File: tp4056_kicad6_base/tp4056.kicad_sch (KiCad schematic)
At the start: 33 parts, among them J1 Conn_01x01_Female, J2 Conn_01x01_Female, J3 USB_B_Micro, J4 Conn_01x02_Male, J6 Conn_01x05_Male, Q1 AO3401A, Q2 FS8205A, Q3 AO3401A, U1 TP4056, U2 DW01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

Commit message: SCH. Add USB and Wall Power Adaptor
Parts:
- added D4: MBR1020VL, Diode_SMD_AKL:D_SOD-123F, symbol Diode:MBR1020VL
- added Q4: AO3401A, Package_TO_SOT_SMD_AKL:SOT-23, symbol Transistor_FET:AO3401A
- added Q5: AO3400A, Package_TO_SOT_SMD_AKL:SOT-23, symbol Transistor_FET:AO3400A
- added R10: 10k, Resistor_SMD:R_0805_2012Metric, symbol Device:R
- added R11: 1k, Resistor_SMD:R_0805_2012Metric, symbol Device:R
- R3: value 10k -> 2k
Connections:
- net Earth: now also Q5.2 (S), R11.1
- net Rprog: now reaches R3.1, U1.2 (PROG)
- net Rprog: now also R10.1
- net VBUS renamed VCC
- net VCC: now also D4.1 (K), Q4.2 (S); no longer J1.1 (Pin_1), J3.1 (VBUS)
- new net: Q5.3 (D), R10.2
- new net Vusb: J3.1 (VBUS), Q4.3 (D)
- new net Vwall: D4.2 (A), J1.1 (Pin_1), Q4.1 (G), Q5.1 (G), R11.2
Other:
- note added: "Corriente de carga diferencias USB y Entrada CC [TP4054 datasheet]"
- note added: "USB + Wall Adapter"

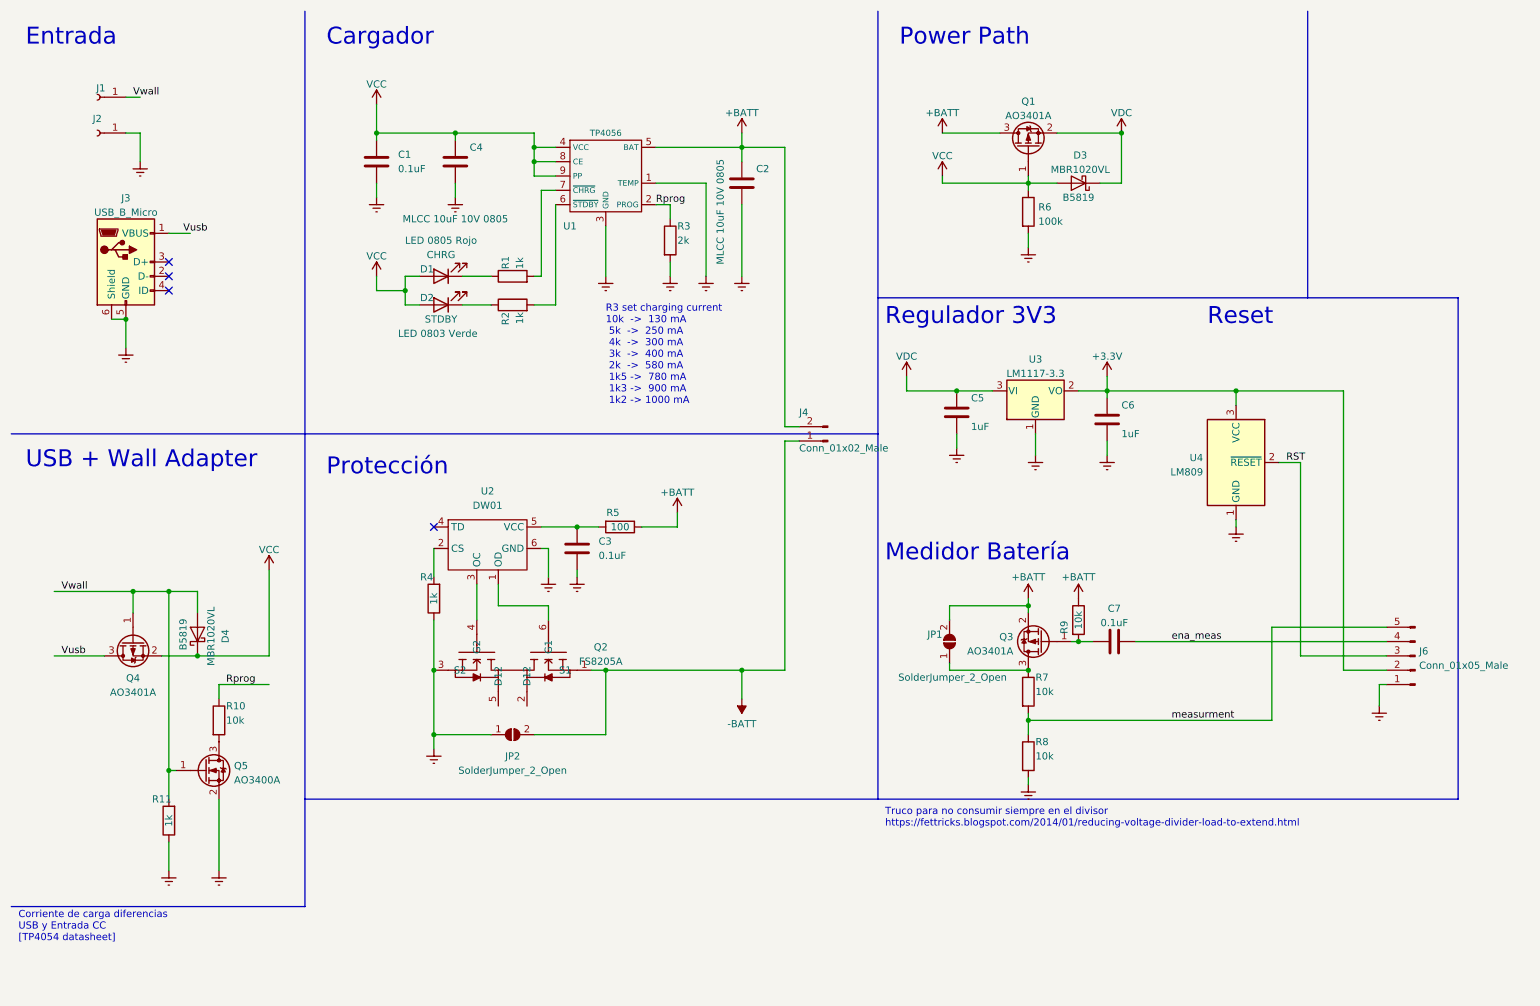
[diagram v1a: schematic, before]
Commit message: PCB. 40x25. Add wall adpapter option. To final check.
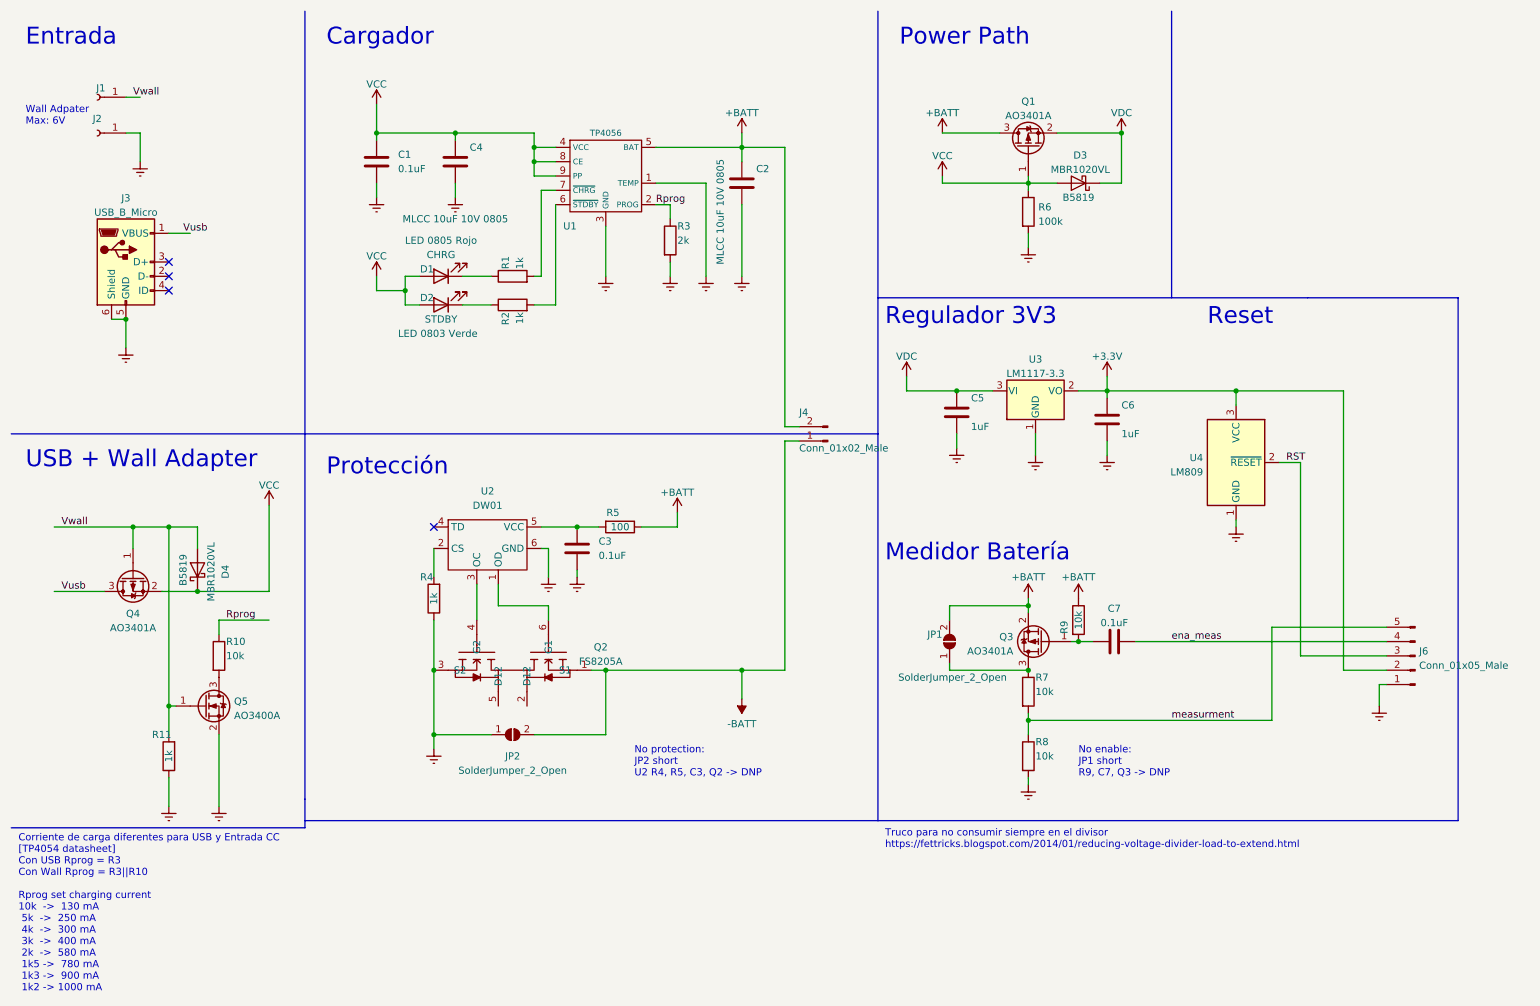
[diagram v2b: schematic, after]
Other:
- note added: "Corriente de carga diferentes para USB y Entrada CC [TP4054 datasheet] Con USB Rprog = R3 Con Wall Rprog = R3||R10 Rprog set charging current 10k -> 130 mA 5k -> 250 mA 4k -> 300 mA 3k -> 400 mA 2k -> 580 mA 1k5 -> 780 mA 1k3 -> 900 mA 1k2 -> 1000 mA"
- note added: "No enable: JP1 short R9, C7, Q3 -> DNP"
- note added: "No protection: JP2 short U2 R4, R5, C3, Q2 -> DNP"
- note added: "Wall Adpater Max: 6V"
- note removed: "Corriente de carga diferencias USB y Entrada CC [TP4054 datasheet]"
- note removed: "R3 set charging current 10k -> 130 mA 5k -> 250 mA 4k -> 300 mA 3k -> 400 mA 2k -> 580 mA 1k5 -> 780 mA 1k3 -> 900 mA 1k2 -> 1000 mA"
- company: (none) -> LUXIS S.A.
- title: Batery charger w/TP4056, protect and power path -> Batery charger w/accesories
- moved on the sheet: D4, Q4, Q5, R10, R11

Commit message: PCB. output files. minor cosmetic changes.
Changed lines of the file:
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@@
     (stroke (width 0) (type default) (color 0 0 0 0))
   )
-  (polyline (pts (xy 267.97 156.21) (xy 267.97 63.5))
+  (polyline (pts (xy 267.97 157.48) (xy 267.97 63.5))
     (stroke (width 0) (type default) (color 0 0 0 0))
   )
@@
     (stroke (width 0) (type default) (color 0 0 0 0))
   )
-  (polyline (pts (xy 165.1 156.21) (xy 267.97 156.21))
+  (polyline (pts (xy 165.1 157.48) (xy 267.97 157.48))
     (stroke (width 0) (type default) (color 0 0 0 0))
   )
@@
     (stroke (width 0) (type default) (color 0 0 0 0))
   )
-  (polyline (pts (xy 165.1 156.21) (xy 165.1 87.63))
+  (polyline (pts (xy 165.1 157.48) (xy 165.1 87.63))
     (stroke (width 0) (type default) (color 0 0 0 0))
   )
@@
     (stroke (width 0) (type default) (color 0 0 0 0))
   )
-  (polyline (pts (xy 63.5 156.21) (xy 165.1 156.21))
+  (polyline (pts (xy 63.5 157.48) (xy 165.1 157.48))
     (stroke (width 0) (type default) (color 0 0 0 0))
   )
@@
   )
   (text "Truco para no consumir siempre en el divisor\nhttps://fettricks.blogspot.com/2014/01/reducing-voltage-divider-load-to-extend.html"
-    (at 166.37 161.29 0)
+    (at 166.37 162.56 0)
     (effects (font (size 1.27 1.27)) (justify left bottom))
   )
